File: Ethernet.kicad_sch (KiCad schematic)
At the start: 9 parts, among them IC6 LAN8651B1-E_LMX, J7 RJ45_LED, Y4 Crystal_GND24

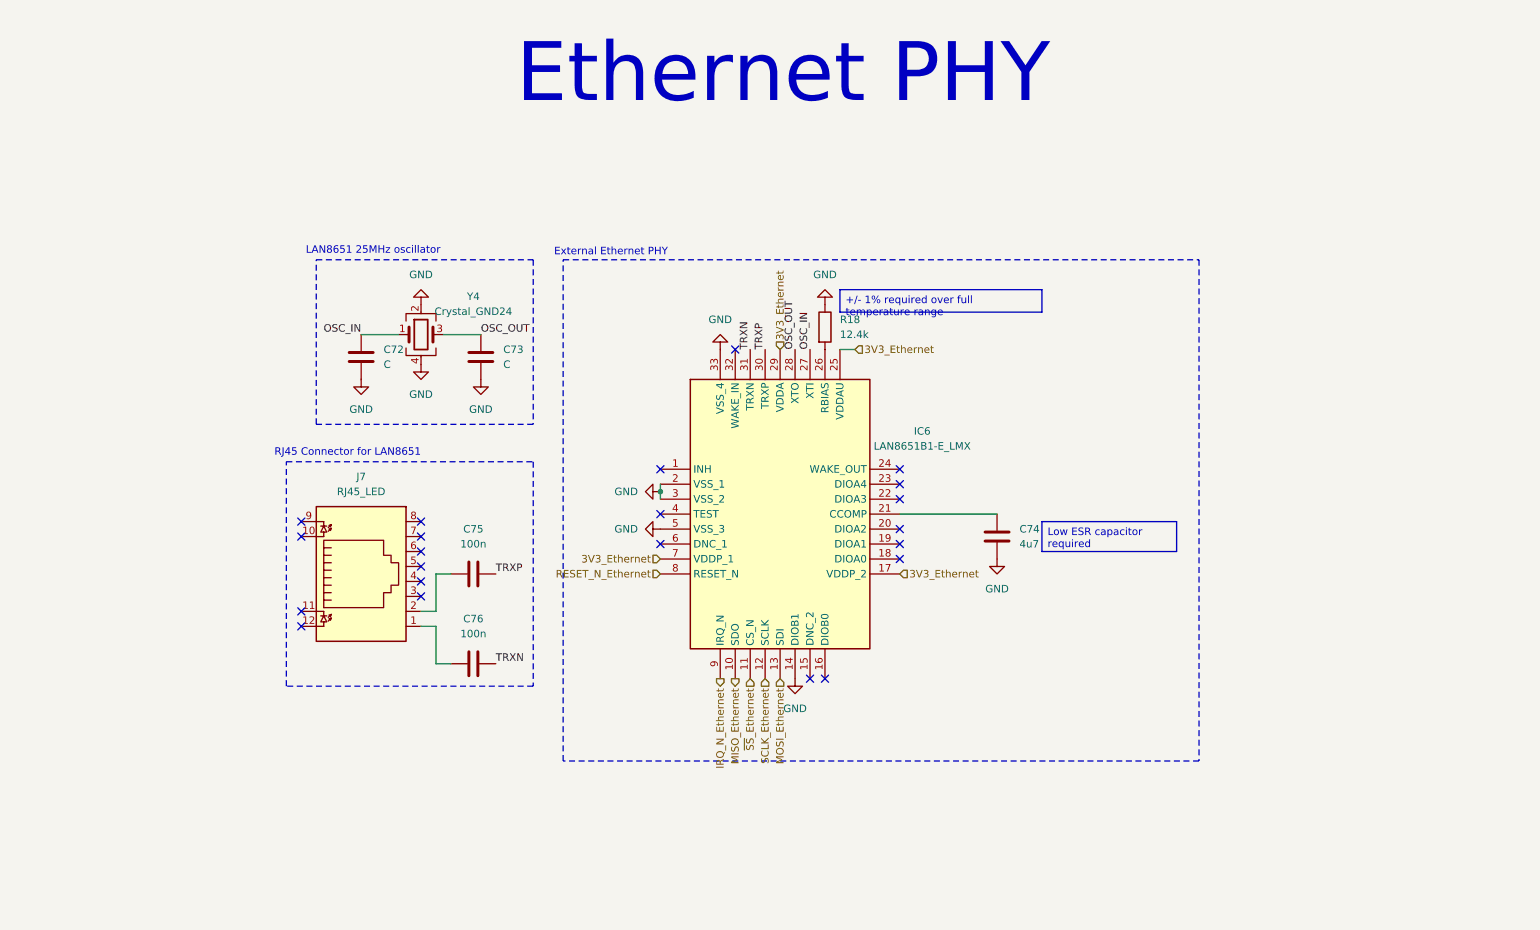
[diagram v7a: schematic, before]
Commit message: Finish ethernet schematic and add second LDO for wake/sleep of ETH
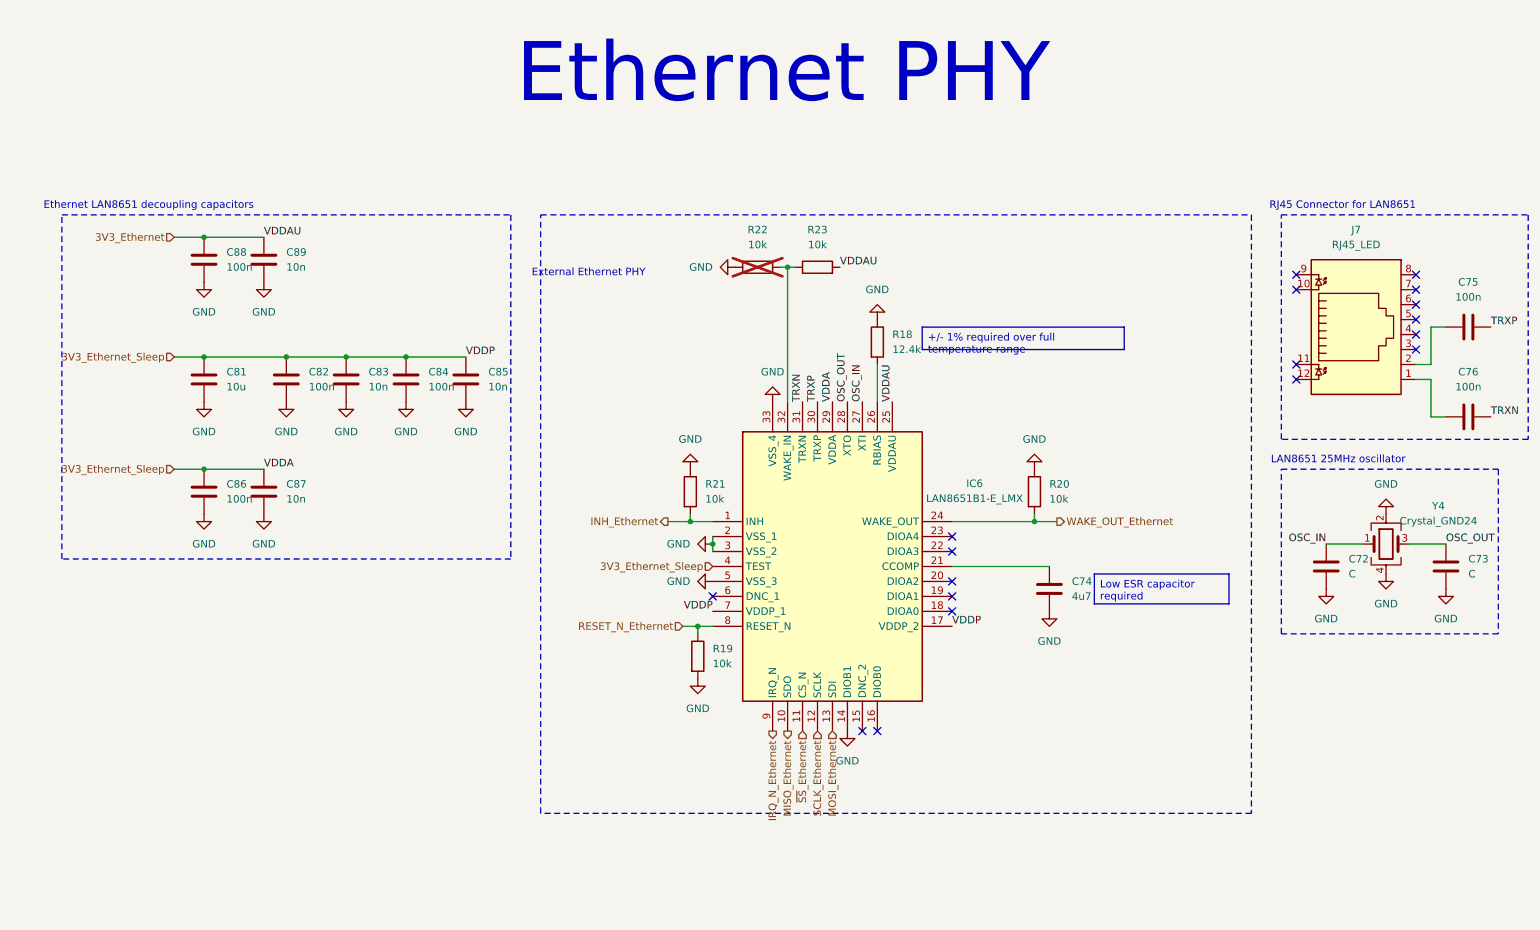
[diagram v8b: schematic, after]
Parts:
- added C81: 10u, symbol Device:C
- added C82, C84, C86, C88: 100n, symbol Device:C
- added C83, C85, C87, C89: 10n, symbol Device:C
- added R19, R20, R21, R22, R23: 10k, symbol Device:R
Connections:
- net 3V3_Ethernet: now also C88.1, C89.1, R23.2; no longer IC6.17 (VDDP_2), IC6.29 (VDDA), IC6.7 (VDDP_1)
- net GND: now also C81.2, C82.2, C83.2, C84.2, C85.2, C86.2, C87.2, C88.2, C89.2, R19.2, R20.1, R21.1, R22.1
- net RESET_N_Ethernet: now also R19.1
- net INH_Ethernet: now reaches IC6.1 (INH)
- net INH_Ethernet: now also R21.2
- net WAKE_OUT_Ethernet: now reaches IC6.24 (WAKE_OUT)
- net WAKE_OUT_Ethernet: now also R20.2
- net at IC6.32 (WAKE_IN): now also R22.2, R23.1
- net 3V3_Ethernet_Sleep: now reaches IC6.4 (TEST)
- net 3V3_Ethernet_Sleep: now also IC6.17 (VDDP_2), IC6.29 (VDDA), IC6.7 (VDDP_1), C81.1, C82.1, C83.1, C84.1, C85.1, C86.1, C87.1
- no-connect marks 22 -> 18
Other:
- note added: "Ethernet LAN8651 decoupling capacitors"
- moved on the sheet: C72, C73, C74, C75, C76, IC6, J7, R18, Y4
